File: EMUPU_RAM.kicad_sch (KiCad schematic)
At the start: 30 parts, among them J1 Conn_01x20_Socket, J2 Conn_01x20_Socket, J3 Barrel_Jack_Switch, J4 Conn_01x06_Pin, J5 Conn_01x08_Pin, J6 Conn_01x06_Pin, J7 Conn_01x02_Pin, SW1 SW_SPDT, SW2 SW_SPST, U1 PIC18F57Q43-IPT, U2 HM678127_SOJ32_Arranged

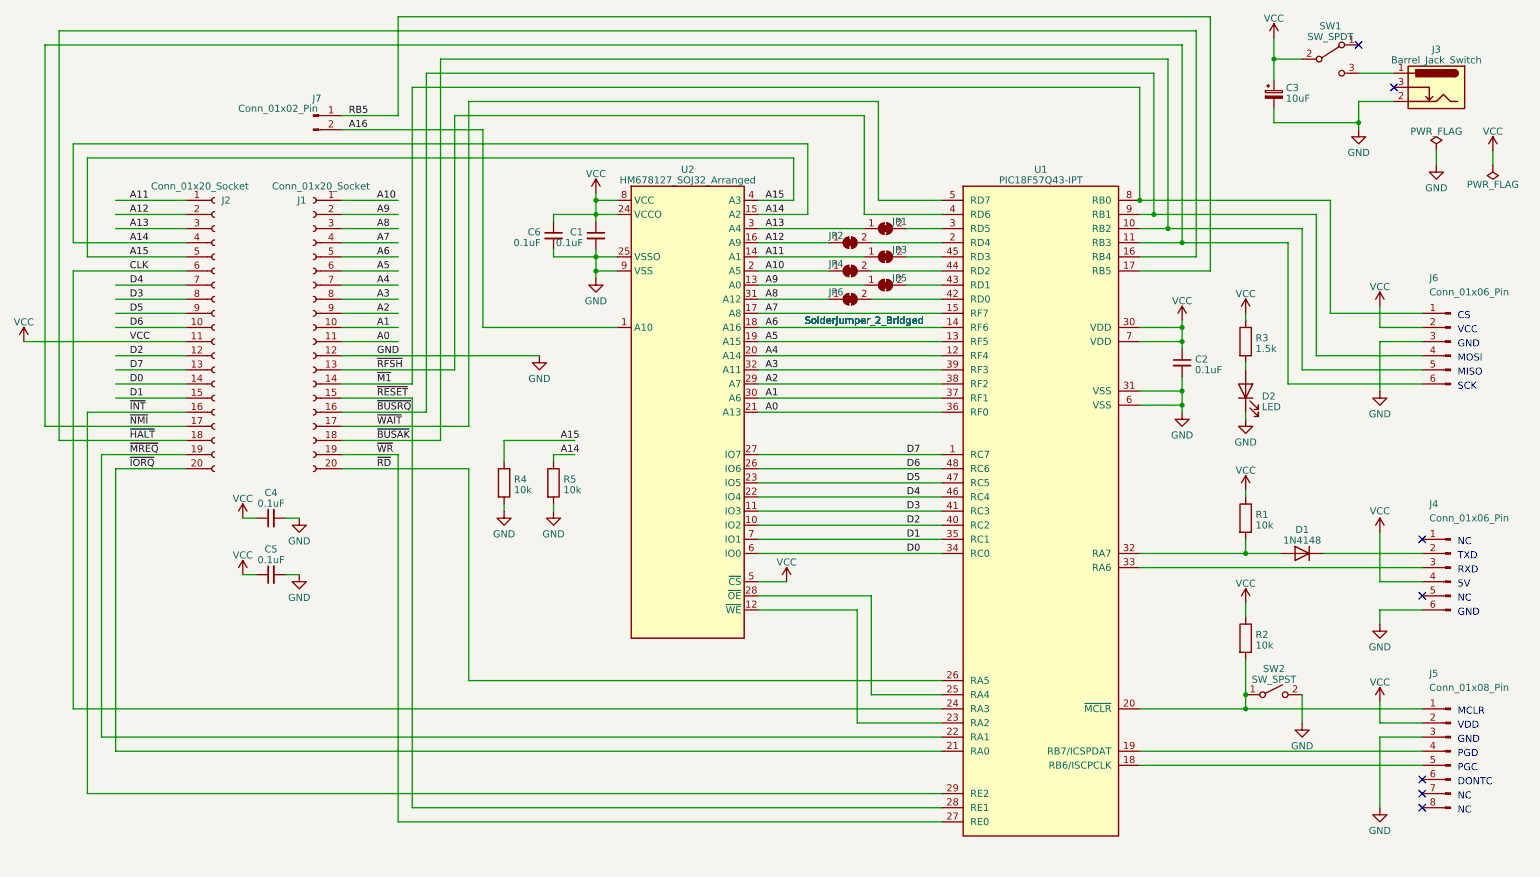
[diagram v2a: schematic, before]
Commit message: Ordered version, designated as Rev. 001
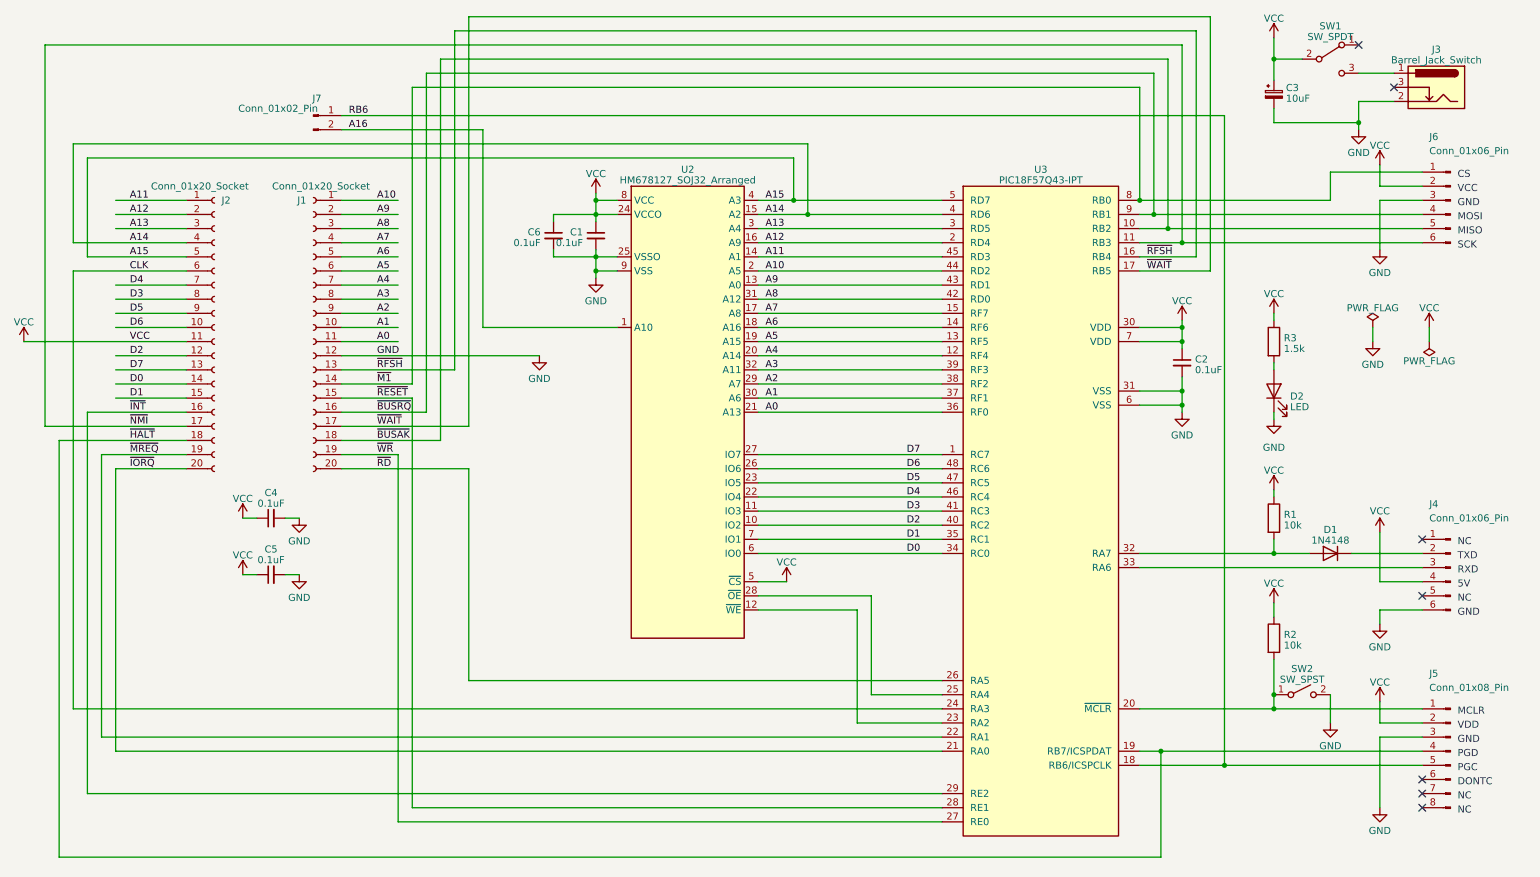
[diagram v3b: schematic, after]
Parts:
- removed JP1, JP2, JP3, JP4, JP5, JP6: SolderJumper_2_Bridged, Jumper:SolderJumper-2_P1.3mm_Bridged_RoundedPad1.0x1.5mm, symbol Jumper:SolderJumper_2_Bridged
- removed R4, R5: 10k, Resistor_THT:R_Axial_DIN0204_L3.6mm_D1.6mm_P7.62mm_Horizontal, symbol Device:R
- removed U1: PIC18F57Q43-IPT, 0-local:Quad-2x6, symbol 0-local:PIC18F57Q43-IPT
- added U3: PIC18F57Q43-IPT, 0-local:Quad-2x6, symbol 0-local:PIC18F57Q43-IPT
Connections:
- net RB5 is gone; now on net RB6: J7.1 (Pin_1)
- net A0: now also U3.36 (RF0)
- net A1: now also U3.37 (RF1)
- net A10: now also U3.44 (RD2)
- net A11: now also U3.45 (RD3)
- net A12: now also U3.2 (RD4)
- net A13: now also U3.3 (RD5)
- net A14: now also U3.4 (RD6)
- net A15: now also U3.5 (RD7)
- net A2: now also U3.38 (RF2)
- net A3: now also U3.39 (RF3)
- net A4: now also U3.12 (RF4)
- net A5: now also U3.13 (RF5)
- net A6: now also U3.14 (RF6)
- net A7: now also U3.15 (RF7)
- net A8: now also U3.42 (RD0)
- net A9: now also U3.43 (RD1)
- net CLK: now also U3.24 (RA3)
- net D0: now also U3.34 (RC0)
- net D1: now also U3.35 (RC1)
- net D2: now also U3.40 (RC2)
- net D3: now also U3.41 (RC3)
- net D4: now also U3.46 (RC4)
- net D5: now also U3.47 (RC5)
- net D6: now also U3.48 (RC6)
- net D7: now also U3.1 (RC7)
- net GND: now also U3.31 (VSS), U3.6 (VSS)
- net VCC: now also U3.30 (VDD), U3.7 (VDD)
- net ~{BUSAK}: now also U3.10 (RB2)
- net ~{BUSRQ}: now also U3.9 (RB1)
- net ~{HALT}: now also J5.4 (Pin_4), U3.19 (RB7/ICSPDAT)
- net ~{INT}: now also U3.29 (RE2)
- net ~{IORQ}: now also U3.21 (RA0)
- net ~{M1}: now also U3.8 (RB0)
- net ~{MREQ}: now also U3.22 (RA1)
- net ~{NMI}: now also U3.11 (RB3)
- net ~{RD}: now also U3.26 (RA5)
- net ~{RESET}: now also U3.28 (RE1)
- net ~{RFSH}: now also U3.16 (RB4)
- net ~{WAIT}: now also U3.17 (RB5)
- net ~{WR}: now also U3.27 (RE0)
- net at J5.1 (Pin_1), R2.2, SW2.1 (A): now also U3.20 (~{MCLR})
- net RB6: now reaches J5.5 (Pin_5)
- net RB6: now also U3.18 (RB6/ICSPCLK)
- net at D1.2 (A), R1.2: now also U3.32 (RA7)
- net at U2.12 (~{WE}): now also U3.23 (RA2)
- net at U2.28 (~{OE}): now also U3.25 (RA4)
- net at J4.3 (Pin_3): now also U3.33 (RA6)
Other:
- moved on the sheet: D1, D2, J6, R1, R2, R3, SW2

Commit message: Fix BARREL_JACK footpattern, modify schematic file (Rev002), pcb file fix ongoing
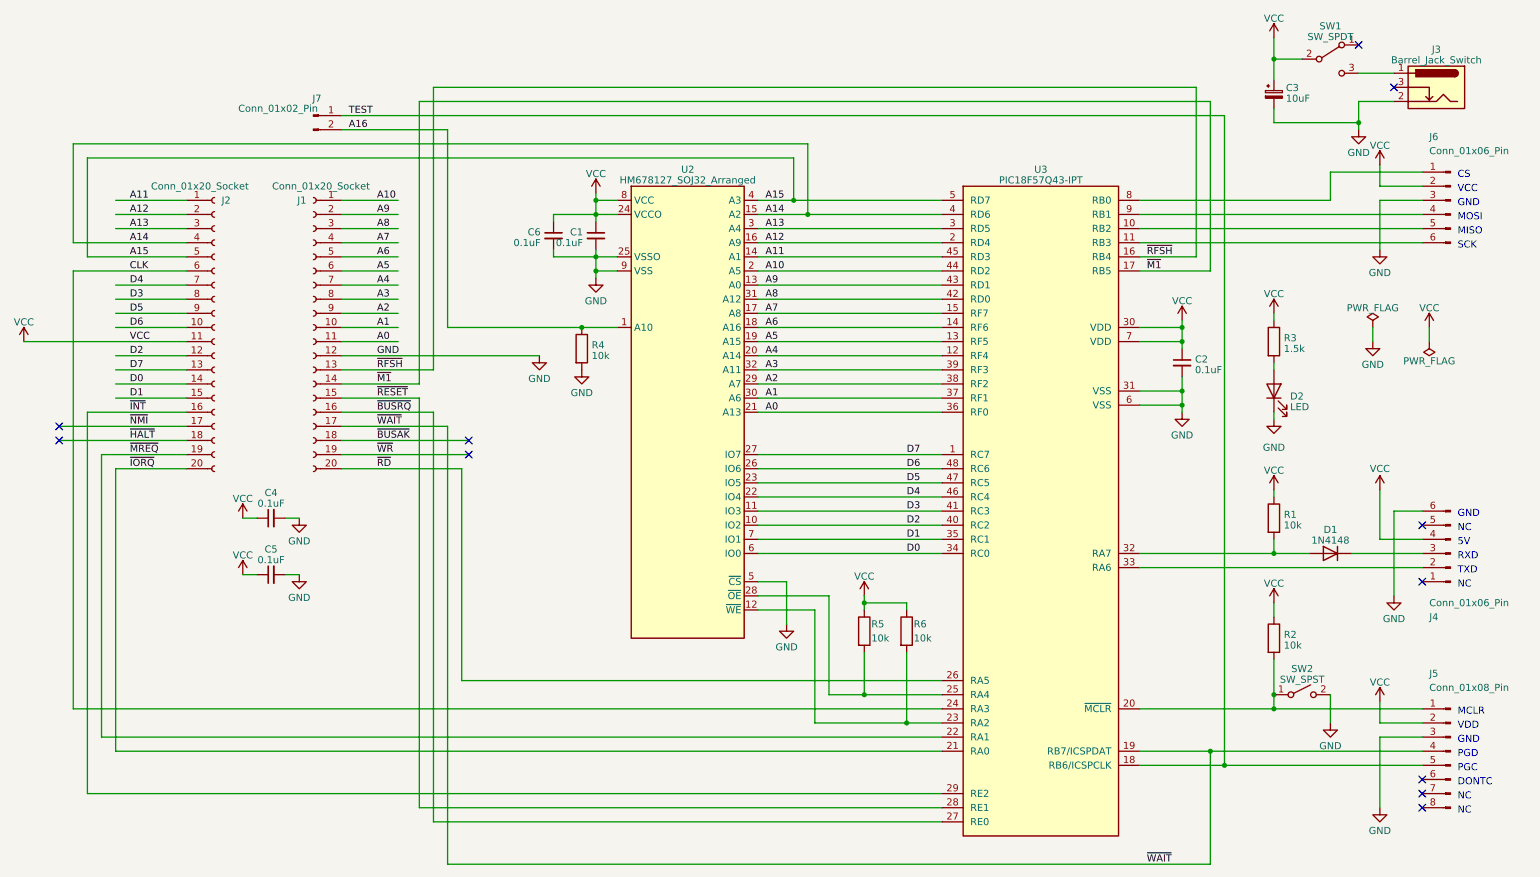
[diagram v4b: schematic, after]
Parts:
- added R4, R5, R6: 10k, Resistor_THT:R_Axial_DIN0204_L3.6mm_D1.6mm_P7.62mm_Horizontal, symbol Device:R
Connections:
- net A16: now also R4.1
- net GND: now also U2.5 (~{CS}), R4.2
- net VCC: now also R5.1, R6.1; no longer U2.5 (~{CS})
- net ~{BUSAK}: no longer J6.5 (Pin_5), U3.10 (RB2)
- net ~{BUSRQ}: now also U3.27 (RE0); no longer J6.4 (Pin_4), U3.9 (RB1)
- net ~{HALT}: no longer J5.4 (Pin_4), U3.19 (RB7/ICSPDAT)
- net ~{M1}: now also U3.17 (RB5); no longer J6.1 (Pin_1), U3.8 (RB0)
- net ~{NMI}: no longer J6.6 (Pin_6), U3.11 (RB3)
- net ~{WAIT}: now also J5.4 (Pin_4), U3.19 (RB7/ICSPDAT); no longer U3.17 (RB5)
- net ~{WR}: no longer U3.27 (RE0)
- net at D1.1 (K): now also J4.3 (Pin_3); no longer J4.2 (Pin_2)
- net at U3.33 (RA6): now also J4.2 (Pin_2); no longer J4.3 (Pin_3)
- net at U2.12 (~{WE}), U3.23 (RA2): now also R6.2
- net at U2.28 (~{OE}), U3.25 (RA4): now also R5.2
- net RB6 renamed TEST
- new net: J6.1 (Pin_1), U3.8 (RB0)
- new net: J6.4 (Pin_4), U3.9 (RB1)
- new net: J6.5 (Pin_5), U3.10 (RB2)
- new net: J6.6 (Pin_6), U3.11 (RB3)
- no-connect marks 7 -> 11
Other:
- title: EMUPU_RAM board -> EMUPU_RAM48 board
- moved on the sheet: J4
